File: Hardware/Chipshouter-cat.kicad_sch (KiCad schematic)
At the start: 72 parts

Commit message: Finished routing
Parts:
- removed D6: (no value), symbol Diode:MBR340
- added D4: MBR120, Diode_SMD:D_SOD-123, symbol Diode:MBR340
- added Q1: DMG3415U-7, Package_TO_SOT_SMD:SOT-23, symbol Device:Q_PMOS_GSD
- added R14: 100K, Resistor_SMD:R_0603_1608Metric, symbol Device:R_Small
- C1, C3: value (none) -> 4.7uF; footprint (none) -> Capacitor_SMD:C_0805_2012Metric
- C10, C8: value (none) -> 27pF; footprint (none) -> Capacitor_SMD:C_0603_1608Metric
- C11, C12, C14, C15, C16, C17, C18, C19, C20, C7: value (none) -> 0.1uF; footprint (none) -> Capacitor_SMD:C_0402_1005Metric
- C13, C9: value (none) -> 1uF; footprint (none) -> Capacitor_SMD:C_0603_1608Metric
- C2: value (none) -> 100nF; footprint (none) -> Capacitor_SMD:C_0603_1608Metric; Manf# C0603C104K5RAC7867 -> C0603C104K5RACTU
- C4: value (none) -> 0.47uF; footprint (none) -> chipshouter:CAPC6153X500N; Manf# CGA9P1X7T2J474K250KE -> KRM55TR72J474MH01K
- C5, C6: value (none) -> 10uF; footprint (none) -> Capacitor_SMD:C_0402_1005Metric
- D1, D10, D2, D3: value (none) -> SM4005PL-TP; footprint (none) -> Diode_SMD:D_SOD-123F
- D4: value (none) -> MURA160T3G; footprint (none) -> Diode_SMD:D_SMA
- D5: value (none) -> MM3Zxx; footprint (none) -> Diode_SMD:D_SOD-323F
- D7: value (none) -> H.V.Detected; footprint (none) -> LED_SMD:LED_0603_1608Metric
- D8: value (none) -> Status; footprint (none) -> LED_SMD:LED_0603_1608Metric
- D9: value (none) -> Charge On; footprint (none) -> LED_SMD:LED_0603_1608Metric
- F1: value (none) -> 0.5A; footprint (none) -> Fuse:Fuse_0805_2012Metric
- J1: value (none) -> Antenna; footprint (none) -> Rf:SMA_EDGE
- J2: value (none) -> BG306-02-A-2-0400-L-G; footprint (none) -> chipshouter:BG30602A20400LG
- J3: value (none) -> Header7; footprint (none) -> Connector_PinHeader_2.54mm:PinHeader_1x07_P2.54mm_Vertical
- J4: value (none) -> Header 2; footprint (none) -> Connector_PinHeader_2.54mm:PinHeader_1x02_P2.54mm_Vertical
- J5: value (none) -> Header 4; footprint (none) -> Connector_PinHeader_2.54mm:PinHeader_1x04_P2.54mm_Vertical
- J6: value (none) -> Input Power:2x AA Battery; footprint (none) -> Connector_PinHeader_2.54mm:PinHeader_1x02_P2.54mm_Vertical
- P1: value (none) -> USB_C_Plug_USB2.0; footprint (none) -> Connectors:C393939
- Q1, Q2: value (none) -> AO3422; footprint (none) -> Package_TO_SOT_SMD:SOT-23; symbol IRLML0060TRPBF:IRLML0060TRPBF -> Transistor_FET:AO3400A
- Q3: value (none) -> LDA111STR; footprint (none) -> chipshouter:SOP254P952X470-6N
- Q4: value (none) -> RGT16BM65DTL; footprint (none) -> Package_TO_SOT_SMD:TO-252-3_TabPin2
- R1, R9: value (none) -> 10R; footprint (none) -> Resistor_SMD:R_0603_1608Metric
- R10: value (none) -> 20M; footprint (none) -> Resistor_SMD:R_2010_5025Metric
- R11: value (none) -> 300K; footprint (none) -> chipshouter:RESC6432X120N
- R13, R14, R16, R5, R6: value (none) -> 1K; footprint (none) -> Resistor_SMD:R_0603_1608Metric
- R17: value (none) -> 10K; footprint (none) -> Resistor_SMD:R_0603_1608Metric
- R18: value (none) -> 1k; footprint (none) -> Resistor_SMD:R_0603_1608Metric
- R19, R20: value (none) -> 27; footprint (none) -> Resistor_SMD:R_0603_1608Metric
- R2, R4: value (none) -> 5.1K; footprint (none) -> Resistor_SMD:R_0603_1608Metric
- R3: value (none) -> 75R; footprint (none) -> Resistor_SMD:R_0805_2012Metric
- R7: value (none) -> 22K; footprint (none) -> Resistor_SMD:R_0603_1608Metric
- R8: value (none) -> 2K; footprint (none) -> Resistor_SMD:R_0805_2012Metric
- SW1: value (none) -> TL3342F450QG; footprint (none) -> Button_Switch_SMD:SW_SPST_TL3342; Manf# TL3301AF160QJ -> TL3342F450QG
- SW2: value (none) -> ON; footprint (none) -> chipshouter:OS102011MA1QN1
- SW3, SW6: value (none) -> TL3342F450QG; footprint (none) -> Button_Switch_SMD:SW_SPST_TL3342; Manf# KSC741JLFS -> TL3342F450QG
- SW4: value (none) -> RESET; footprint (none) -> Button_Switch_SMD:SW_SPST_TL3342
- SW5: value (none) -> BOOT; footprint (none) -> Button_Switch_SMD:SW_SPST_TL3342
- T1, T2: value (none) -> ATB322524; footprint (none) -> chipshouter:ATB3225240110T000; symbol ATB322524-0110-T000:ATB322524-0110-T000 -> Device:Transformer_1P_1S
- U1: value (none) -> AP2112K-3.3; footprint (none) -> Package_TO_SOT_SMD:SOT-23-5
- U2: value (none) -> W25Q16JV; footprint (none) -> chipshouter:W25Q16JVUUIQ
- U3: value (none) -> RP2040; footprint (none) -> chipshouter:RP2040-QFN-56
- Y1: value (none) -> 12Mhz; footprint (none) -> Crystal:Crystal_SMD_5032-2Pin_5.0x3.2mm
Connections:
- net VCC is gone; now on net +3V3: D1.2 (A), J5.2 (Pin_2), R7.1, SW6.2
- net +3V3: now also C6.1, U1.5 (VOUT); no longer D10.1 (K)
- net GND: now also R14.2
- net VBUS: now also D4.2 (A), Q1.1 (G), R14.1; no longer SW2.1 (A)
- net -: now reaches R20.2, U3.46 (USB_DM)
- net +: now reaches R19.2, U3.47 (USB_DP)
- net GP14 renamed HVPULSE
- net GP20 renamed HVPWM
- new net: D4.1 (K), Q1.2 (S), SW2.1 (A)
- new net VSYS: D10.1 (K), Q1.3 (D)
- no-connect marks 2 -> 17
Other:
- moved on the sheet: C5, C6, R19, R20, SW2, U1

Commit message: BOM_generated
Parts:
- D4: Manf# MBR120LSF -> (none)
- J1: footprint Rf:SMA_EDGE -> chipshouter:732511150
- J6: footprint Connector_PinHeader_2.54mm:PinHeader_1x02_P2.54mm_Vertical -> chipshouter:JST_S2B-PH-K-S(LF)(SN); LCSC# (none) -> C173752; Proveedor (none) -> LCSC
- R14: LCSC# C15458 -> C100048; Manf# WR06X104JTL -> (none)
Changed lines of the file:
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@@
       (effects (font (size 1.27 1.27)) hide)
     )
-    (property "Manf#" "MBR120LSF" (at 139.7 267.97 0)
+    (property "Manf#" "" (at 139.7 267.97 0)
       (effects (font (size 1.27 1.27)) hide)
     )
@@
       (effects (font (size 1.27 1.27)) hide)
     )
-    (property "LCSC#" "C15458" (at 130.81 274.32 0)
+    (property "LCSC#" "C100048" (at 130.81 274.32 0)
       (effects (font (size 1.27 1.27)) hide)
     )
-    (property "Manf#" "WR06X104JTL" (at 130.81 274.32 0)
+    (property "Manf#" "" (at 130.81 274.32 0)
       (effects (font (size 1.27 1.27)) hide)
     )
@@
       (effects (font (size 1.27 1.27)) (justify left))
     )
-    (property "Footprint" "Rf:SMA_EDGE" (at 146.685 61.595 0)
+    (property "Footprint" "chipshouter:732511150" (at 146.685 61.595 0)
       (effects (font (size 1.27 1.27)) hide)
     )
@@
       (effects (font (size 1.27 1.27)) (justify left))
     )
-    (property "Footprint" "Connector_PinHeader_2.54mm:PinHeader_1x02_P2.54mm_Vertical" (at 368.3 47.625 0)
+    (property "Footprint" "chipshouter:JST_S2B-PH-K-S(LF)(SN)" (at 368.3 47.625 0)
       (effects (font (size 1.27 1.27)) hide)
     )
@@
       (effects (font (size 1.27 1.27)) hide)
     )
+    (property "LCSC#" "C173752" (at 368.3 47.625 0)
+      (effects (font (size 1.27 1.27)) hide)
+    )
+    (property "Proveedor" "LCSC" (at 368.3 47.625 0)
+      (effects (font (size 1.27 1.27)) hide)
+    )

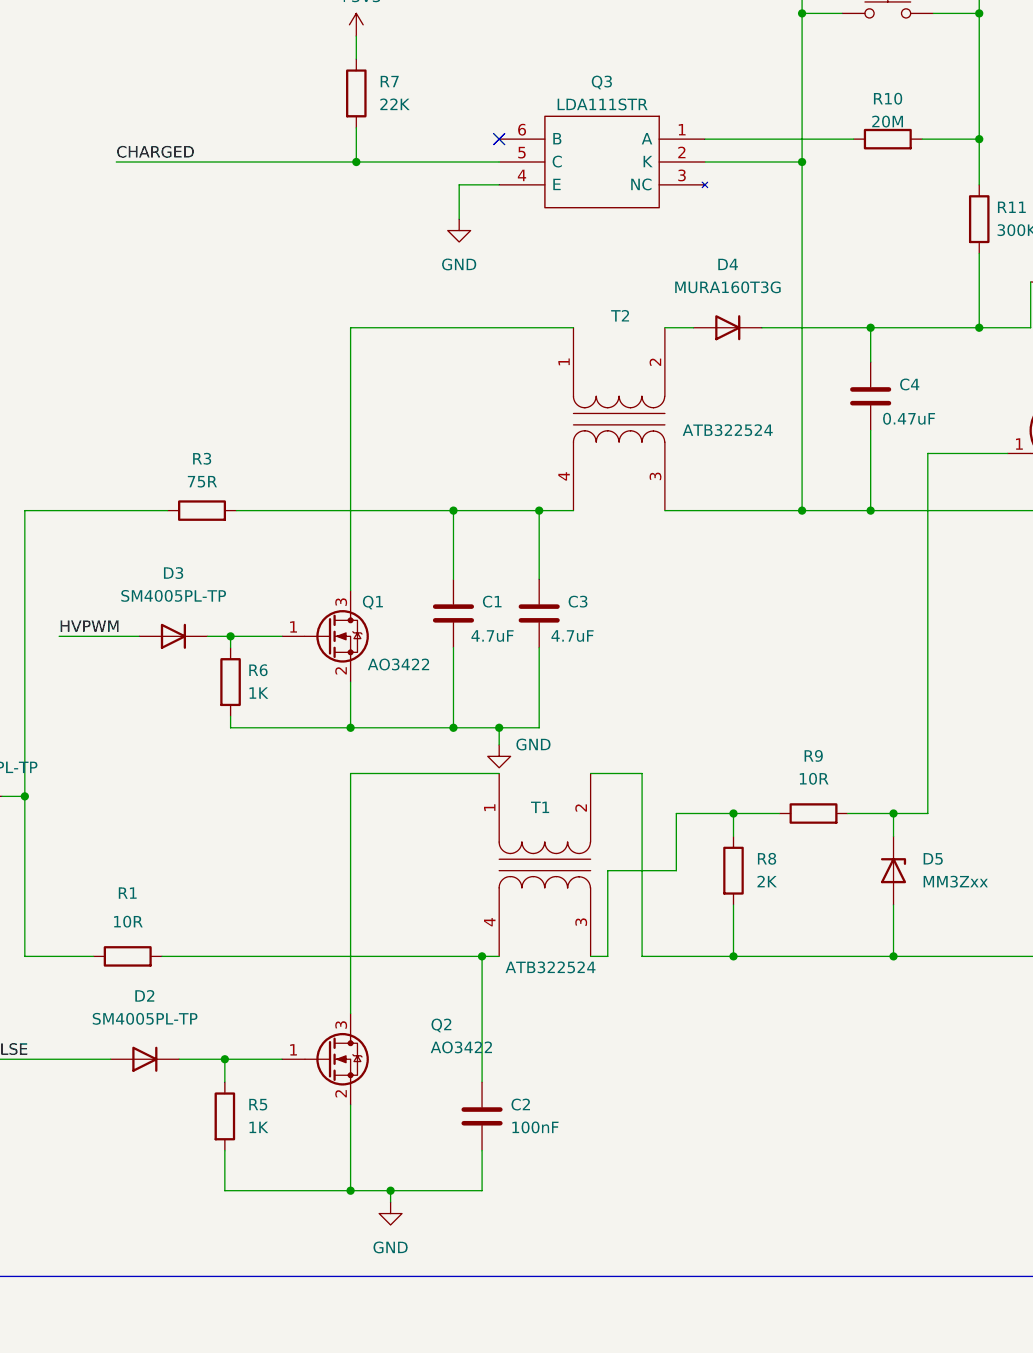
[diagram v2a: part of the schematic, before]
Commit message: Transformer symbols changed
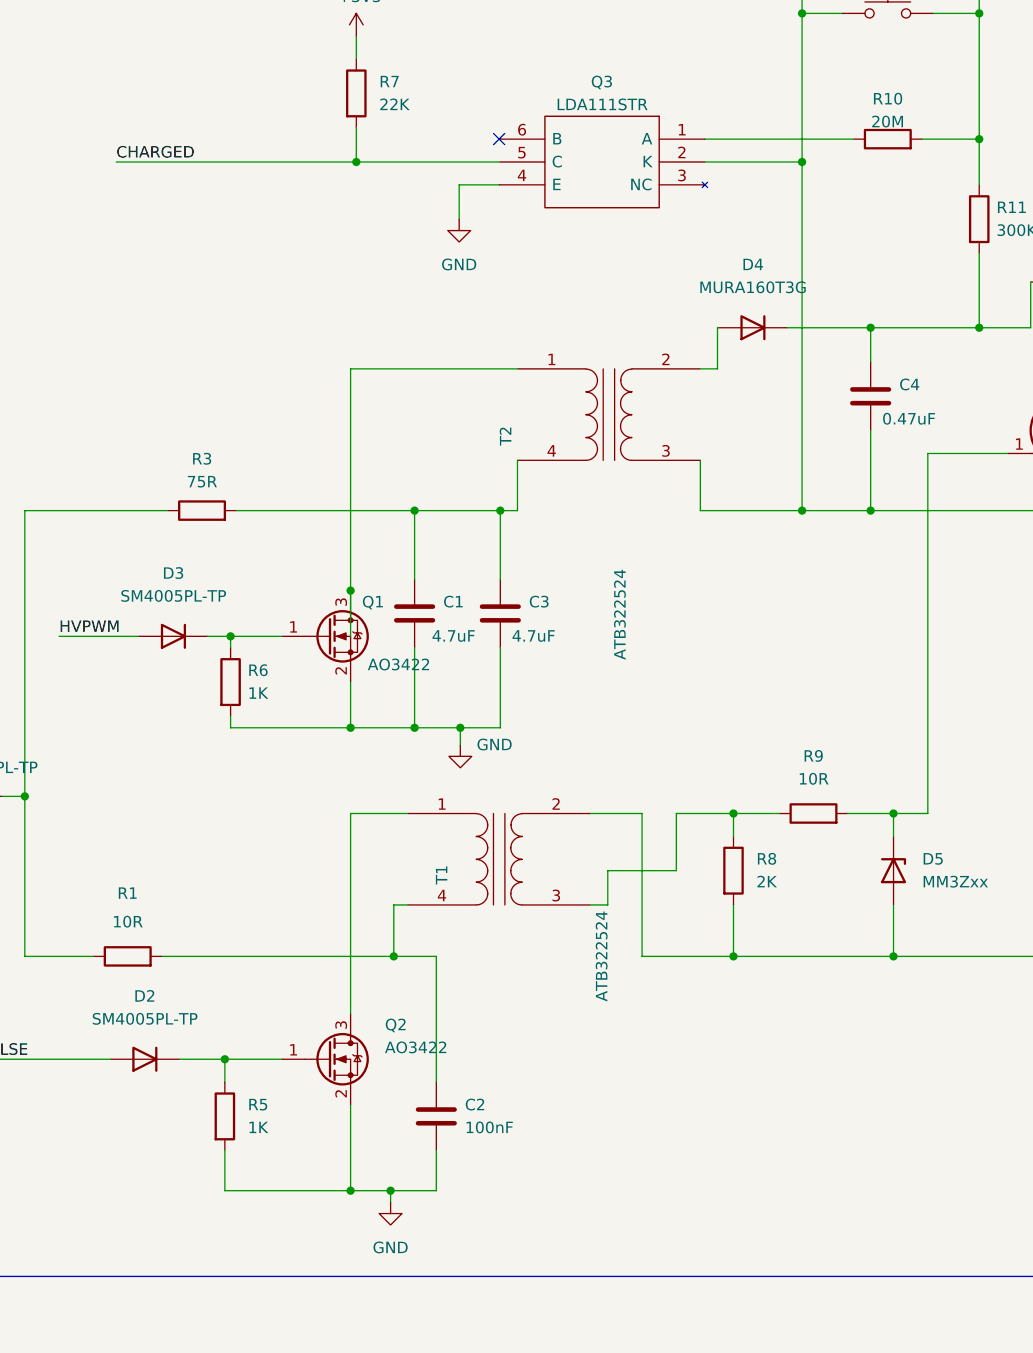
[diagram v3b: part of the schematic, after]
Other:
- moved on the sheet: C1, C2, C3, D4, T1, T2
